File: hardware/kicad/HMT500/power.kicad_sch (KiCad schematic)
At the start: 21 parts, among them U1 TPS26600PWPR, U2 LMR36006, U3 TPS7A2033PDBVR

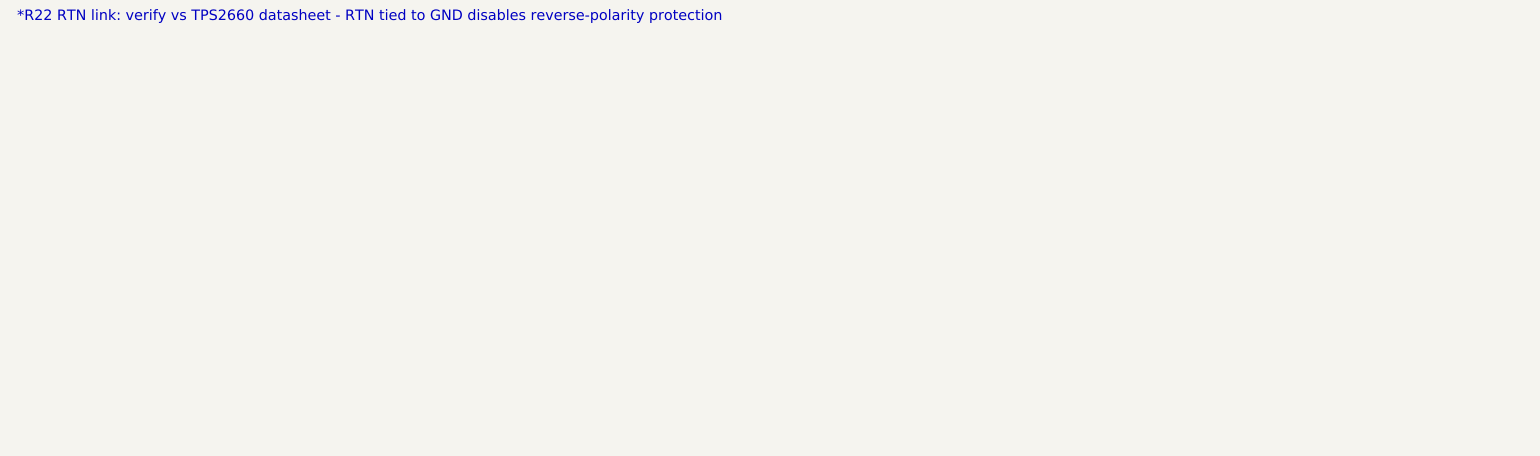
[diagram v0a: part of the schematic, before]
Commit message: Schematic: key-parts table (role, features, specs) on every sheet
- Aligned 4-column table per sheet: reference, part, role, features/specs;
  values still to confirm against datasheets marked with *
- Connector and RS-485 sheets moved to A3 for room
- New checks: text and boxes stay inside the page and out of the title block;
  every character of Hangul text must exist in NanumGothic (minus sign and micro
  sign substituted)

Co-Authored-By: Claude Opus 5.5 <noreply@anthropic.com>
Claude-Session: https://claude.ai/code/session_01JA2o8uJsqp9Vzsg4b665ev
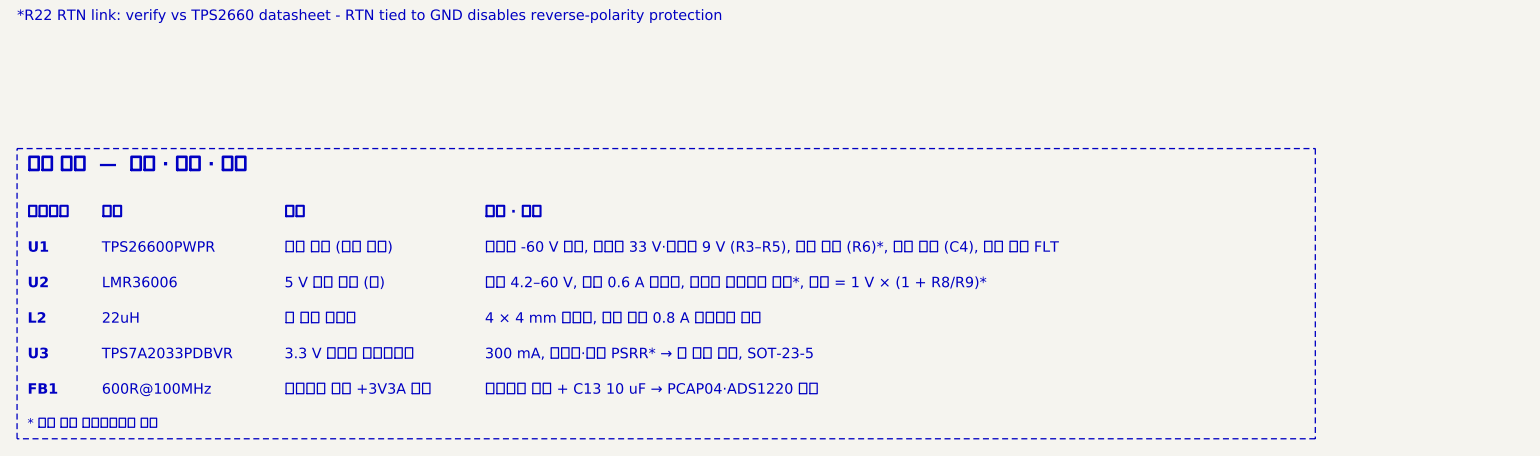
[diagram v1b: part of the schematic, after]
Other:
- note added: "* 표시 값은 데이터시트로 확인"
- note added: "22uH"
- note added: "3.3 V 저잡음 레귤레이터"
- note added: "300 mA, 저잡음·높은 PSRR* → 벅 리플 제거, SOT-23-5"
- note added: "4 × 4 mm 차폐형, 포화 전류 0.8 A 이상으로 선정"
- note added: "5 V 강압 전원 (벅)"
- note added: "600R@100MHz"
- note added: "FB1"
- note added: "L2"
- note added: "LMR36006"
- note added: "TPS26600PWPR"
- note added: "TPS7A2033PDBVR"
- note added: "U1"
- note added: "U2"
- note added: "U3"
- note added: "벅 출력 인덕터"
- note added: "부품"
- note added: "부품번호"
- note added: "아날로그 전원 +3V3A 분리"
- note added: "역극성 -60 V 차단, 과전압 33 V·저전압 9 V (R3–R5), 전류 제한 (R6)*, 돌입 제한 (C4), 고장 출력 FLT"
- note added: "역할"
- note added: "입력 4.2–60 V, 출력 0.6 A 동기식, 무부하 소비전류 작음*, 출력 = 1 V × (1 + R8/R9)*"
- note added: "전자 퓨즈 (입력 보호)"
- note added: "주요 부품 — 역할 · 특징 · 사양"
- note added: "특징 · 사양"
- note added: "페라이트 비드 + C13 10 uF → PCAP04·ADS1220 전원"
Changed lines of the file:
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@@
 (rectangle (start 172.72 66.04) (end 279.4 119.38) (stroke (width 0.1524) (type dash) (color 72 72 160 1)) (fill (type none)))
 (rectangle (start 284.48 66.04) (end 398.78 119.38) (stroke (width 0.1524) (type dash) (color 72 72 160 1)) (fill (type none)))
+(rectangle (start 25.4 152.4) (end 183.35 187.706) (stroke (width 0.1524) (type dash) (color 72 72 160 1)) (fill (type none)))
 (text "*R22 RTN link: verify vs TPS2660 datasheet - RTN tied to GND disables reverse-polarity protection" (at 25.4 137.16 0) (effects (font (size 1.27 1.27)) (justify left bottom)))
 (text "eFuse  TPS2660   reverse -60 V  /  OVP 33 V  /  UVLO 9 V" (at 26.67 69.088 0) (effects (font (size 1.6 1.6) bold) (justify left bottom)))
@@
 (text "LDO 3.3 V   TPS7A2033   +   analog rail +3V3A" (at 285.75 69.088 0) (effects (font (size 1.6 1.6) bold) (justify left bottom)))
 (text "3.3 V 레귤레이터" (at 371.208 69.088 0) (effects (font (face "NanumGothic") (size 1.4 1.4)) (justify left bottom)))
+(text "부품번호" (at 26.67 161.036 0) (effects (font (face "NanumGothic") (size 1.27 1.27) bold) (justify left bottom)))
+(text "부품" (at 35.7124 161.036 0) (effects (font (face "NanumGothic") (size 1.27 1.27) bold) (justify left bottom)))
+(text "역할" (at 57.9374 161.036 0) (effects (font (face "NanumGothic") (size 1.27 1.27) bold) (justify left bottom)))
+(text "특징 · 사양" (at 82.3214 161.036 0) (effects (font (face "NanumGothic") (size 1.27 1.27) bold) (justify left bottom)))
+(text "U1" (at 26.67 165.354 0) (effects (font (size 1.27 1.27) bold) (justify left bottom)))
+(text "TPS26600PWPR" (at 35.7124 165.354 0) (effects (font (size 1.27 1.27)) (justify left bottom)))
+(text "전자 퓨즈 (입력 보호)" (at 57.9374 165.354 0) (effects (font (face "NanumGothic") (size 1.27 1.27)) (justify left bottom)))
+(text "역극성 -60 V 차단, 과전압 33 V·저전압 9 V (R3–R5), 전류 제한 (R6)*, 돌입 제한 (C4), 고장 출력 FLT" (at 82.3214 165.354 0) (effects (font (face "NanumGothic") (size 1.27 1.27)) (justify left bottom)))
+(text "U2" (at 26.67 169.672 0) (effects (font (size 1.27 1.27) bold) (justify left bottom)))
+(text "LMR36006" (at 35.7124 169.672 0) (effects (font (size 1.27 1.27)) (justify left bottom)))
+(text "5 V 강압 전원 (벅)" (at 57.9374 169.672 0) (effects (font (face "NanumGothic") (size 1.27 1.27)) (justify left bottom)))
+(text "입력 4.2–60 V, 출력 0.6 A 동기식, 무부하 소비전류 작음*, 출력 = 1 V × (1 + R8/R9)*" (at 82.3214 169.672 0) (effects (font (face "NanumGothic") (size 1.27 1.27)) (justify left bottom)))
+(text "L2" (at 26.67 173.99 0) (effects (font (size 1.27 1.27) bold) (justify left bottom)))
+(text "22uH" (at 35.7124 173.99 0) (effects (font (size 1.27 1.27)) (justify left bottom)))
+(text "벅 출력 인덕터" (at 57.9374 173.99 0) (effects (font (face "NanumGothic") (size 1.27 1.27)) (justify left bottom)))
+(text "4 × 4 mm 차폐형, 포화 전류 0.8 A 이상으로 선정" (at 82.3214 173.99 0) (effects (font (face "NanumGothic") (size 1.27 1.27)) (justify left bottom)))
+(text "U3" (at 26.67 178.308 0) (effects (font (size 1.27 1.27) bold) (justify left bottom)))
+(text "TPS7A2033PDBVR" (at 35.7124 178.308 0) (effects (font (size 1.27 1.27)) (justify left bottom)))
+(text "3.3 V 저잡음 레귤레이터" (at 57.9374 178.308 0) (effects (font (face "NanumGothic") (size 1.27 1.27)) (justify left bottom)))
+(text "300 mA, 저잡음·높은 PSRR* → 벅 리플 제거, SOT-23-5" (at 82.3214 178.308 0) (effects (font (face "NanumGothic") (size 1.27 1.27)) (justify left bottom)))
+(text "FB1" (at 26.67 182.626 0) (effects (font (size 1.27 1.27) bold) (justify left bottom)))
+(text "600R@100MHz" (at 35.7124 182.626 0) (effects (font (size 1.27 1.27)) (justify left bottom)))
+(text "아날로그 전원 +3V3A 분리" (at 57.9374 182.626 0) (effects (font (face "NanumGothic") (size 1.27 1.27)) (justify left bottom)))
+(text "페라이트 비드 + C13 10 uF → PCAP04·ADS1220 전원" (at 82.3214 182.626 0) (effects (font (face "NanumGothic") (size 1.27 1.27)) (justify left bottom)))
+(text "주요 부품  —  역할 · 특징 · 사양" (at 26.67 155.448 0) (effects (font (face "NanumGothic") (size 1.6 1.6) bold) (justify left bottom)))
+(text "* 표시 값은 데이터시트로 확인" (at 26.67 186.69 0) (effects (font (face "NanumGothic") (size 1.1 1.1)) (justify left bottom)))
 )
